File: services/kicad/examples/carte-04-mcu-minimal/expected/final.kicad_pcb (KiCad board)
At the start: 2 copper layers, 60 x 45 mm, 15 parts, among them J1 IN_5V, J2 SWD, U1 STM32F103C8T6, U2 AMS1117-3.3

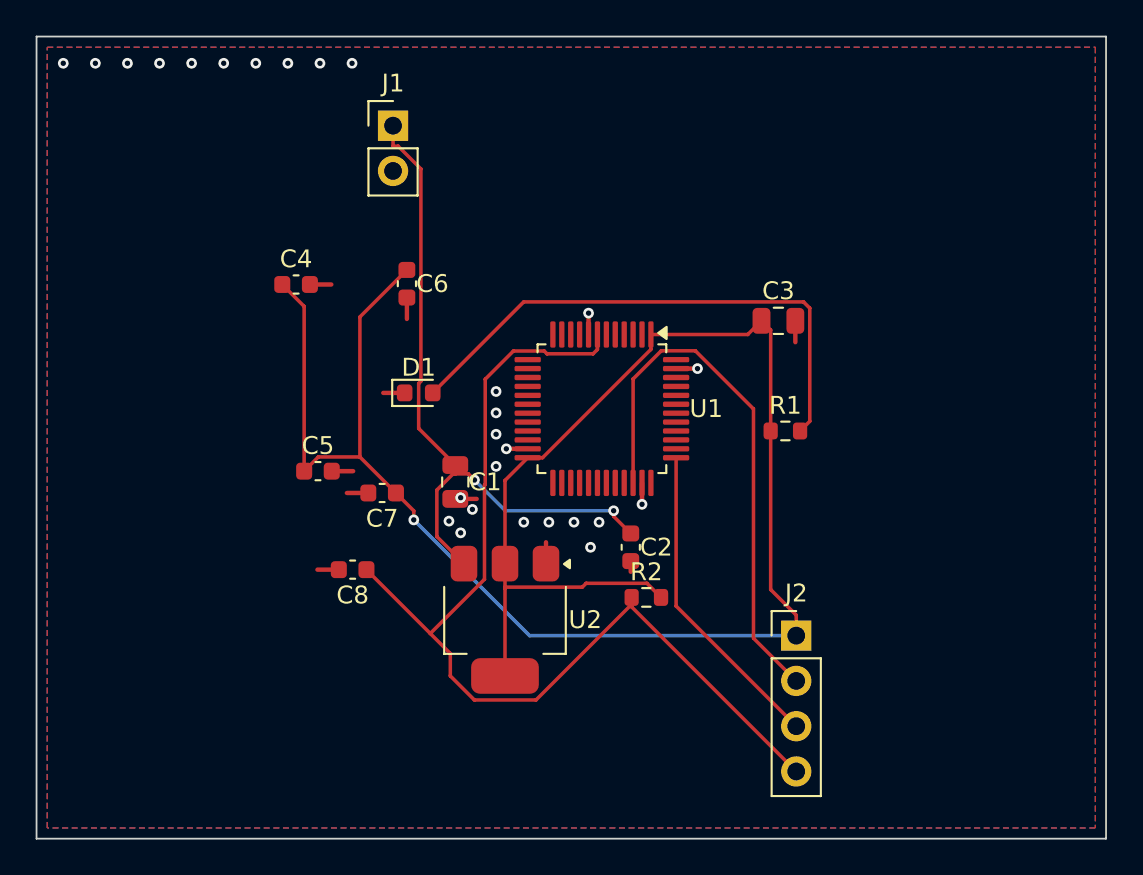
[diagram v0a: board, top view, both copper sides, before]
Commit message: feat(kicad): placement pro et routage 100 % fabricable sur les 16 cartes -- integration sur main (#164)
Branche d'integration coupee depuis origin/main (fab2a82, PR #162) : les
fichiers cles de main etaient des instantanes de feat/placement-seed-snap-
bypass (routing.py = 7981019, placement.py = 437a8b4...). On reprend donc
l'arbre entier de cette branche (345 commits, dernier 9f48667) et on y
conserve ce que main seul apportait :
- tools/verrou_routage.py + son test : « 6,2 Go par routage » rectifie
  (0,2 Go mesure ; c'est la concurrence qui emballe la memoire) ;
- tests/test_driver_llm_resync.py ;
- CLAUDE.md, PLAN.md, DECISIONS.md : fusion a trois voies, les sections
  des deux lignes conservees (2026-09-05 conteneur/verrou, 2026-09-07
  parcours asynchrone et chaine du driver, 2026-09-09/10 lecons).
Les skills *-delegate restent supprimes (remplaces le 2026-08-30).

Contenu : banc en deux phases (placement valide puis routage gele), snap
sur les regles natives, repli GND cible, journal Freerouting incremental,
horloge sans progres, via d'echappement vers le plan principal,
serigraphie degagee ; 16 cartes livrees a 100 %, 0 erreur DRC.

Verification : pytest services/kicad 1805 passed, 16 skipped ;
pnpm type-check 8/8.


Claude-Session: https://claude.ai/code/session_01TnMqm4La2CxQHHB5K8aSSV

Co-authored-by: Claude Fable 5.1 <noreply@anthropic.com>
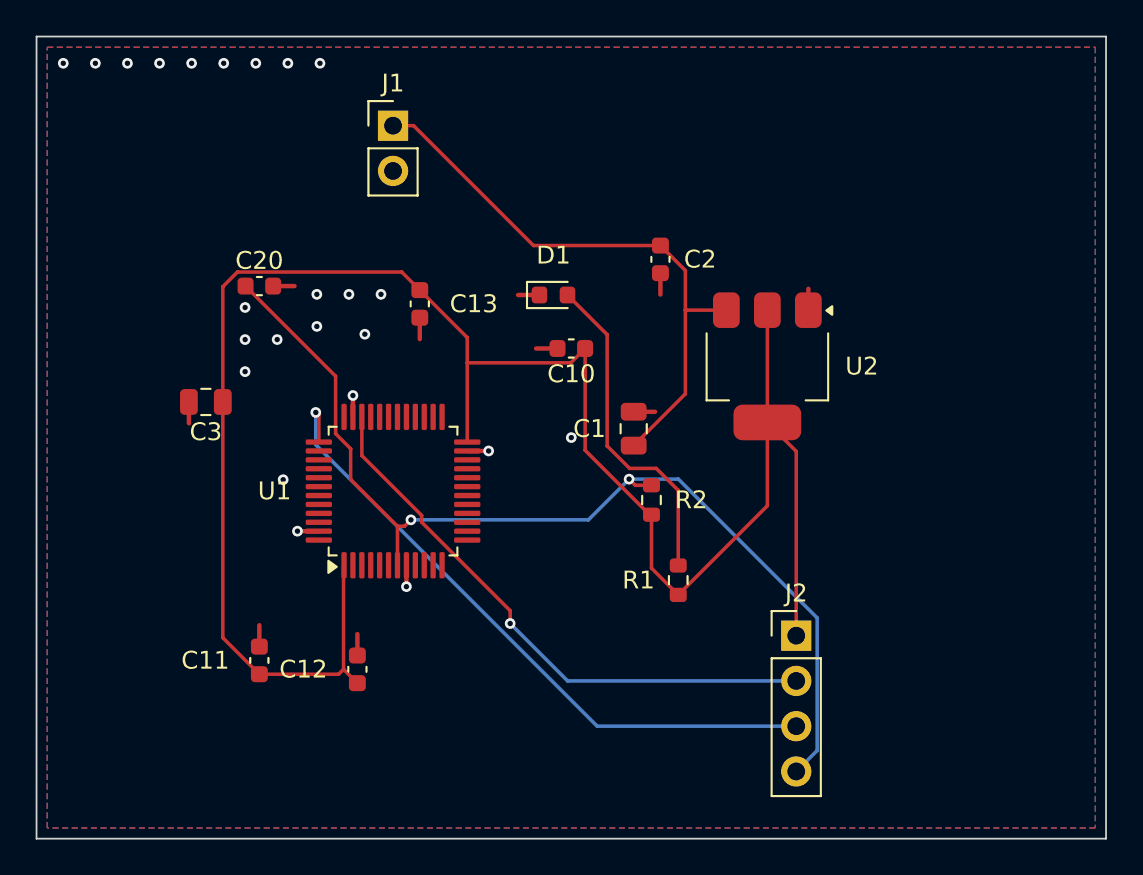
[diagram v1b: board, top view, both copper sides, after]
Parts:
- removed C4, C5, C6, C7, C8: 100nF, C_0603_1608Metric
- added C10: 100nF, C_0603_1608Metric, F.Cu at (148.5, 100.0)
- added C11: 100nF, C_0603_1608Metric, F.Cu at (131.0, 117.5)
- added C12: 100nF, C_0603_1608Metric, F.Cu at (136.5, 118.0)
- added C13: 100nF, C_0603_1608Metric, F.Cu at (140.0, 97.5)
- added C20: 100nF, C_0603_1608Metric, F.Cu at (131.0, 96.5)
- moved C3 32.4 mm to (128.0, 103.0), turned to 180 degrees
- moved U2 20.5 mm to (159.5, 101.0)
- moved C2 16.2 mm to (153.5, 95.0)
- moved U1 12.6 mm to (138.5, 108.0), turned to 90 degrees
- moved C1 10.4 mm to (152.0, 104.5), turned to 90 degrees
- moved R1 10.3 mm to (154.5, 113.0), turned to 90 degrees
- moved D1 9.35 mm to (147.5, 97.0)
- moved R2 5.47 mm to (153.0, 108.5), turned to -90 degrees
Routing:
- net SWCLK: track 17.9 -> 37.0 mm, vias 0 -> 1
- net LED_PWR: track 30.5 -> 18.6 mm
- net VIN: track 38.8 -> 33.1 mm, vias 2 -> 0
- net +3V3: track 112.2 -> 109.5 mm, vias 1 -> 0
- net SWDIO: track 30.8 -> 32.4 mm, vias 0 -> 1
- net GND: track 16.2 -> 16.8 mm, vias 27 -> 24
- net NRST: track 58.1 -> 57.6 mm, vias 0 -> 2

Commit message: test(examples): quatre cartes livrées plus petites — contour resserré mesuré sur le banc (D-2026-09-13-c A)
Banc rejoué en taille heuristique (phase 1 puis phase 2 à placement gelé) :
carte-01 25x20 -> 24,8x17 (84 % de surface), carte-04 60x45 -> 45x44,8
(75 %), carte-06 80x60 -> 65,2x59,8 (81 %), carte-07 110x80 -> 99,5x79,8
(90 %) — toutes 100 % routées, 0 erreur DRC (vérifié en local), rendus 3D
régénérés. Gain nul sur les cartes denses (le génétique remplit la carte) ;
08 et 09 non livrées (dispersion du routage, surface inchangée) ; carte-11
non livrée (carte d'escalade). Tableau complet dans docs/DECISIONS.md.

Co-Authored-By: Claude Fable 5.1 <noreply@anthropic.com>
Claude-Session: https://claude.ai/code/session_01TnMqm4La2CxQHHB5K8aSSV
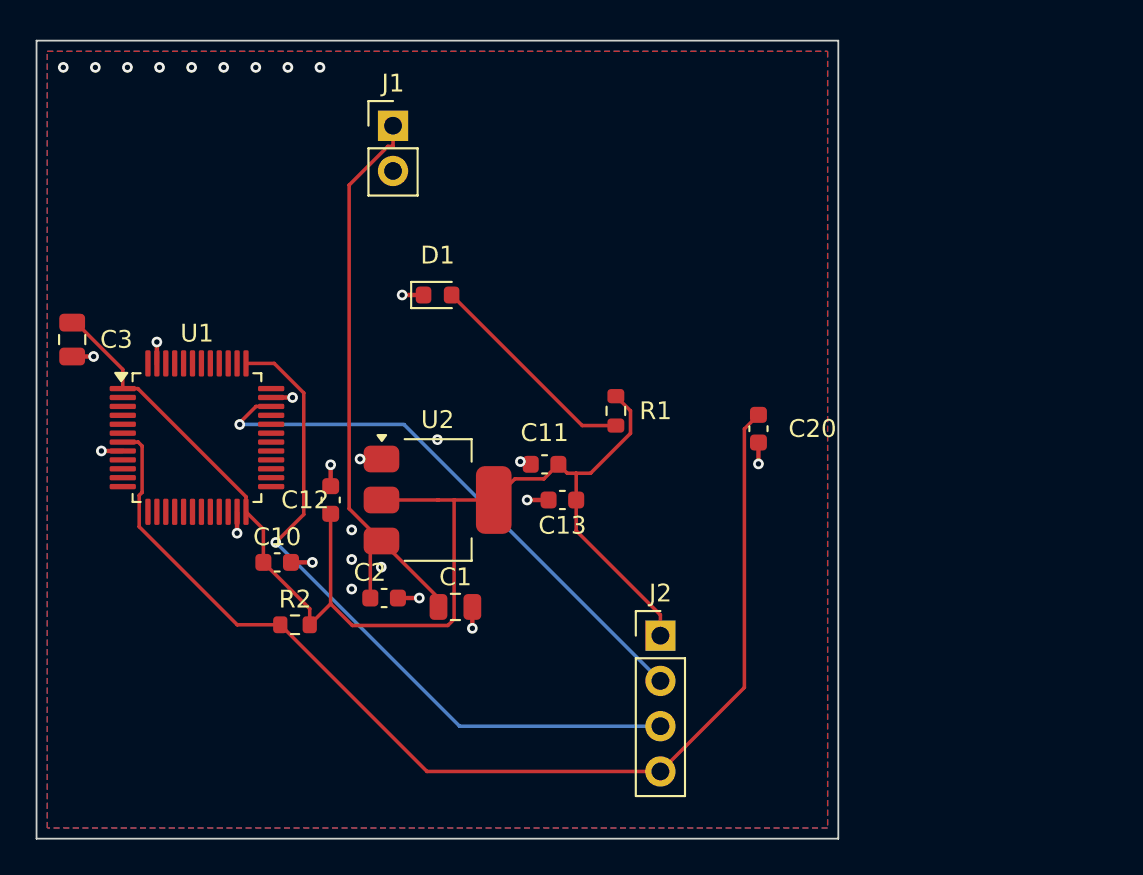
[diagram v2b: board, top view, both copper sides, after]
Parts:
- moved C20 29.1 mm to (159.0, 104.5), turned to -90 degrees
- moved C2 24.5 mm to (138.0, 114.0), turned to 0 degrees
- moved R2 21.2 mm to (133.0, 115.5), turned to 0 degrees
- moved C10 20.4 mm to (132.0, 112.0), turned to 0 degrees
- moved U2 20.0 mm to (141.0, 108.5), turned to 0 degrees
- moved C11 19.4 mm to (147.0, 106.5), turned to 180 degrees
- moved C1 14.1 mm to (142.0, 114.5), turned to 0 degrees
- moved C13 13.6 mm to (148.0, 108.5), turned to 180 degrees
- moved U1 11.4 mm to (127.5, 105.0), turned to 0 degrees
- moved R1 10.1 mm to (151.0, 103.5), turned to -90 degrees
- moved C12 9.62 mm to (135.0, 108.5)
- moved C3 8.28 mm to (120.5, 99.5), turned to -90 degrees
- moved J2 7.62 mm to (153.5, 116.1)
- moved D1 6.50 mm to (141.0, 97.0)
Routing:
- net +3V3: track 109.5 -> 73.5 mm
- net LED_PWR: track 18.6 -> 12.2 mm
- net NRST: track 57.6 -> 63.0 mm, vias 2 -> 0
- net SWCLK: track 37.0 -> 38.8 mm
- net VIN: track 33.1 -> 33.7 mm
- net SWDIO: track 32.4 -> 31.8 mm
- net GND: track 16.8 -> 16.2 mm, vias 24 -> 28
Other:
- board size 60 x 45 mm -> 45 x 44.8 mm

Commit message: chore(banc): relivrer carte-01..10 avec la couture corrigee
Boards reroutes par HTTP depuis placement.kicad_pcb inchange, avec le
code de #217. Juges par remesurer_banc.py : 0 erreur, 0 connexion
manquante sur les dix. 678 -> 443 vias ; la rangee de vias GND du bord
haut a disparu.

mesures.json : `board` recompte, `drc_du_board` rejuge, nouvelle cle
`couture_corrigee` (date, vias_avant, couches). journal.txt et les
champs du run d origine sont laisses tels quels et le disent.
rendu-3d.png : kicad-cli, modeles 3D, iso 1400x900.

Couches d un tirage : huit cartes sur 2, carte-08 et carte-10 sur 4.
CLAUDE.md et BANC_DRIVER_LLM.md recomptes. carte-11 non touchee.

Co-Authored-By: Claude Opus 5 (1M context) <noreply@anthropic.com>
Claude-Session: https://claude.ai/code/session_01TnMqm4La2CxQHHB5K8aSSV
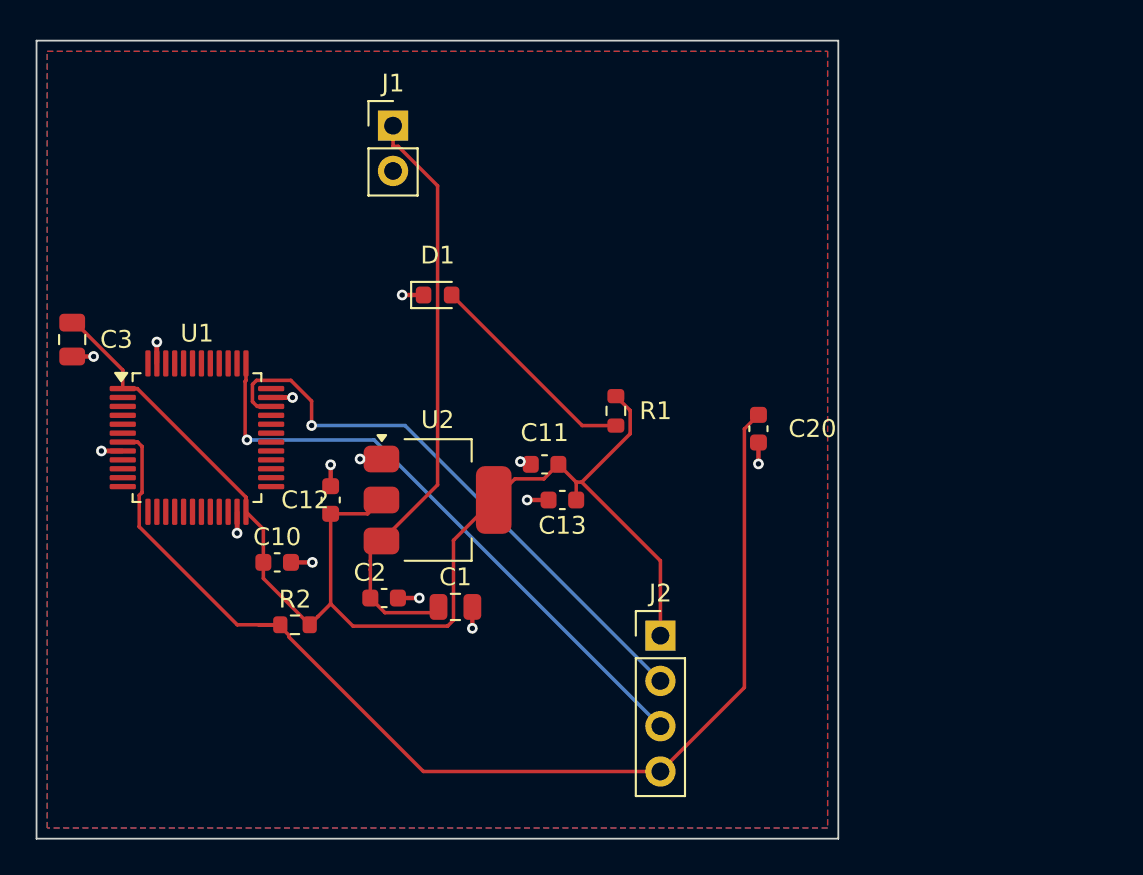
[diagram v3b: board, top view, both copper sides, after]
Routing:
- net GND: track 16.2 -> 21.0 mm, vias 28 -> 14
- net SWCLK: track 38.8 -> 34.2 mm
- net +3V3: track 73.5 -> 72.1 mm
- net NRST: track 63.0 -> 64.2 mm
- net SWDIO: track 31.8 -> 32.9 mm

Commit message: chore(banc): relivrer carte-01/02/04/05 compactes (25 %, D-2026-09-20-a) (#222)
Chaine place -> route rejouee par HTTP sur les dix cartes avec le code de
#220/#221. Quatre sortent a 0 erreur et 0 connexion manquante, sur des
cartes 18 a 58 % plus petites :

  carte-01  24,8x17 -> 20x14      carte-02  55x40 -> 35x25
  carte-04  45x44,8 -> 39x30      carte-05  70x50 -> 46x33

placement.kicad_pcb et final.kicad_pcb remplaces ENSEMBLE ; mesures.json :
board recompte, drc_du_board rejuge (remesurer_banc.py), cle
carte_compacte (tailles et vias d avant, durees, moteur, pistes par
couche). Rendus refaits. Connecteurs a <= 5 mm d un bord (carte-02 J2 :
13,9 -> 3,8 mm) ; carte-05 J3 inchange a 11,4 mm (origine pin 1).

Les six autres gardent leur board du 2026-09-19 : 06 et 08 a 1 manquante,
03 et 07 mauvais, 09 et 10 sans board (tirages figes). Detail dans
BANC_DRIVER_LLM.md. carte-11 non touchee.


Claude-Session: https://claude.ai/code/session_01TnMqm4La2CxQHHB5K8aSSV

Co-authored-by: Claude Fable 5.1 <noreply@anthropic.com>
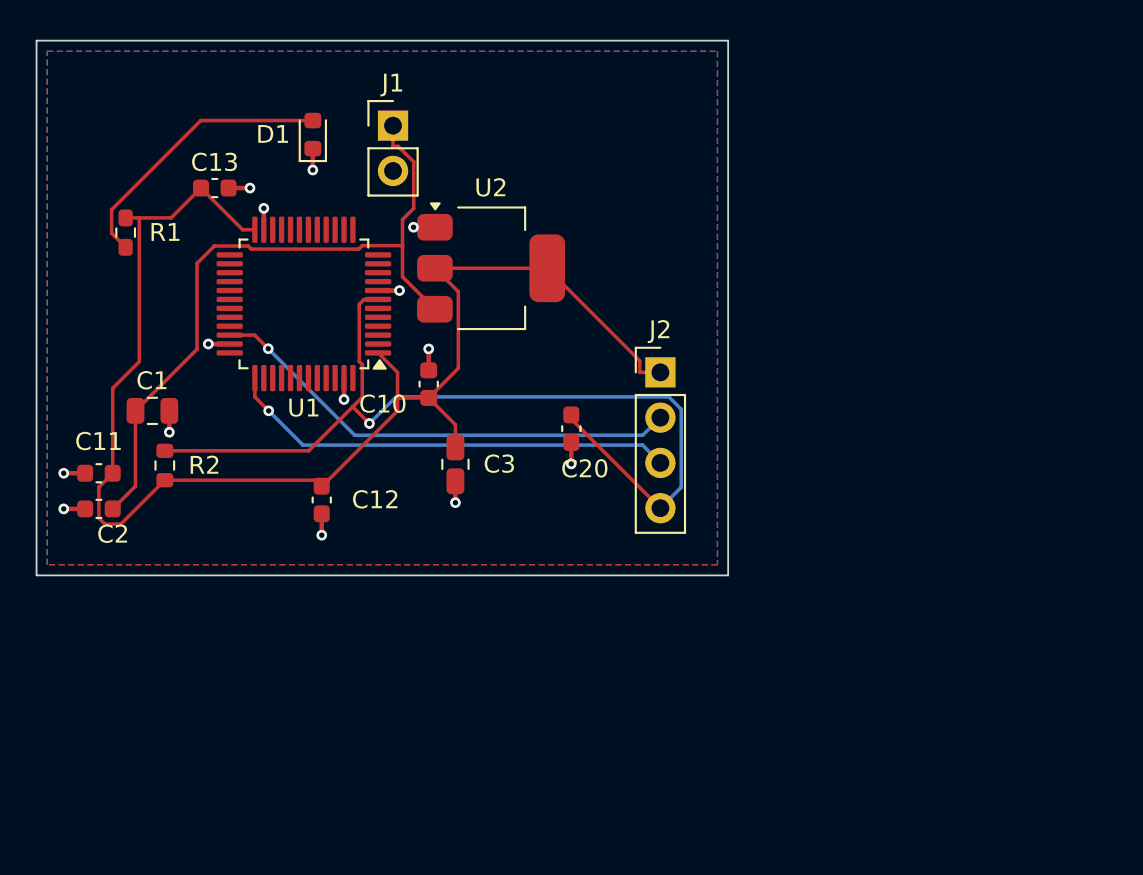
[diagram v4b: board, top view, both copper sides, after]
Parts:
- moved R1 29.3 mm to (123.5, 93.5)
- moved C13 26.2 mm to (128.5, 91.0), turned to 0 degrees
- moved C11 25.0 mm to (122.0, 107.0)
- moved C3 22.6 mm to (142.0, 106.5)
- moved C1 20.2 mm to (125.0, 103.5)
- moved C2 16.8 mm to (122.0, 109.0), turned to 180 degrees
- moved J2 14.8 mm to (153.5, 101.3)
- moved U2 13.3 mm to (144.0, 95.5)
- moved C10 13.1 mm to (140.5, 102.0), turned to 90 degrees
- moved R2 11.5 mm to (125.7, 106.6), turned to -90 degrees
- moved D1 11.4 mm to (134.0, 88.0), turned to 90 degrees
- moved C20 10.5 mm to (148.5, 104.5)
- moved U1 9.60 mm to (133.5, 97.5), turned to 180 degrees
- moved C12 0.50 mm to (134.5, 108.5), turned to -90 degrees
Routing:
- net NRST: track 64.2 -> 51.8 mm, vias 0 -> 1
- net SWCLK: track 34.2 -> 25.3 mm
- net +3V3: track 72.1 -> 79.3 mm
- net VIN: track 33.6 -> 39.8 mm
- net SWDIO: track 32.9 -> 26.9 mm
- net GND: track 21.0 -> 16.8 mm
- net LED_PWR: track 12.2 -> 15.8 mm
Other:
- board size 45 x 44.8 mm -> 38.8 x 30 mm
